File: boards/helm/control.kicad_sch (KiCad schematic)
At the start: 35 parts, among them J11 AS5600, J12 PICO UTIL, J13 THRUST DRV, J22 SERVO MOTOR, U1 Pico 2, U7 BTN8982TA, U8 BTN8982TA

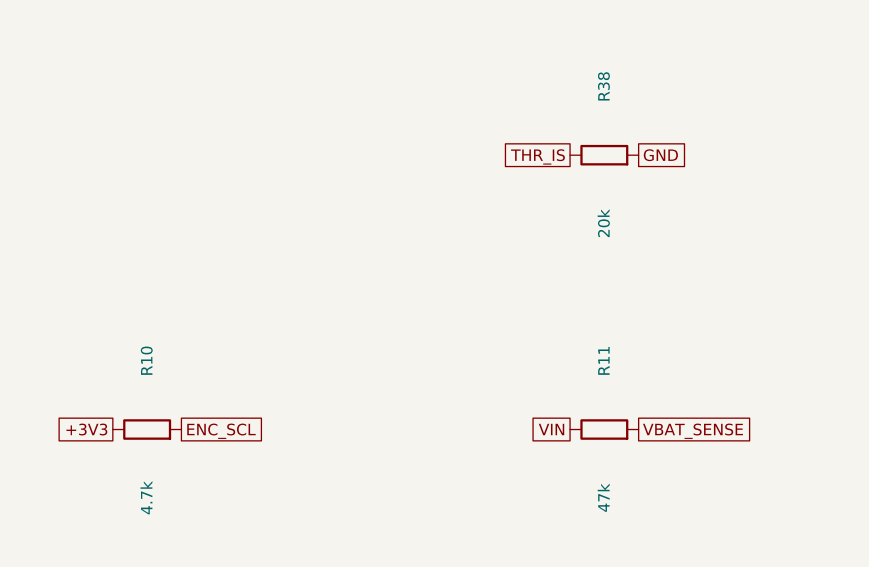
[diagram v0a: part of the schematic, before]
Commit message: feat(helm): steering-zero hall sensor input — J9 grows to 1x3 (5V/GND/SIG), 10k pullup + RC into Pico GP0
Open-collector hall switch (A3144 class) sees a magnet at servo center;
GP0 reads it (also broken out on J12.2; UART0 fallback = GP16/GP1).
Pour-redundant freerouted GND returns near J9/J10 removed. DRC 0/0.

Co-Authored-By: Claude Fable 5 <noreply@anthropic.com>
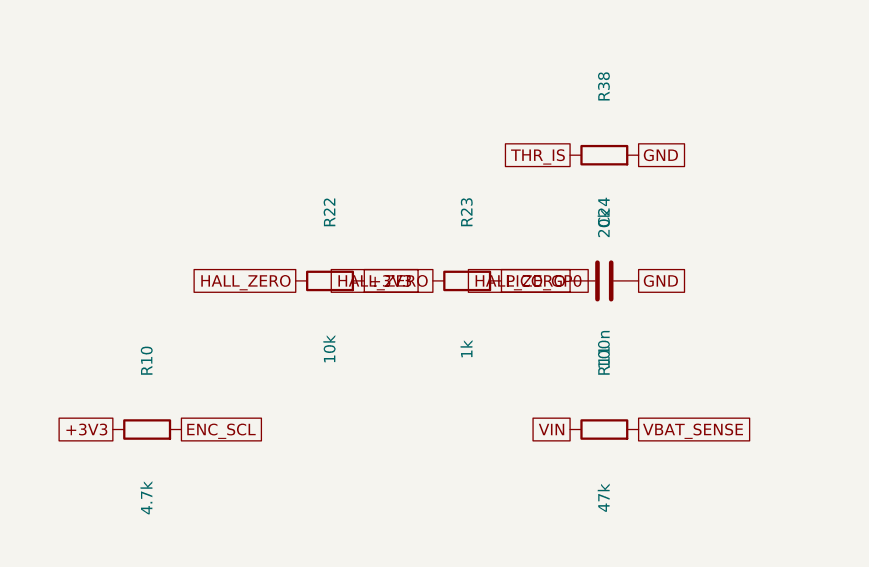
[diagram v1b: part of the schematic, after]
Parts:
- added C24: 100n, Capacitor_SMD:C_0805_2012Metric, symbol Device:C
- added R22: 10k, Resistor_SMD:R_0805_2012Metric, symbol Device:R
- added R23: 1k, Resistor_SMD:R_0805_2012Metric, symbol Device:R
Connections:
- net +3V3: now also R22.2
- net GND: now also C24.2
- net PICO_GP0: now also R23.2
- new net HALL_ZERO: C24.1, R22.1, R23.1
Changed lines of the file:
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@@
     (instances (project "vanchor-helm" (path "/a0000000-0000-4000-8000-000000000001/c0000000-0000-4000-8000-000000000004" (reference "LED5") (unit 1))))
+  )
+  (symbol (lib_id "Device:R") (at 165.1 195.58 90) (unit 1)
+    (exclude_from_sim no) (in_bom yes) (on_board yes) (dnp no)
+    (property "Reference" "R22" (at 165.1 187.96 0)
+      (effects (font (size 1.27 1.27))))
+    (property "Value" "10k" (at 165.1 203.2 0)
+      (effects (font (size 1.27 1.27))))
+    (property "Footprint" "Resistor_SMD:R_0805_2012Metric" (at 165.1 195.58 0)
+      (effects (font (size 1.27 1.27)) (hide yes)))
+    (property "Datasheet" "" (at 165.1 195.58 0)
+      (effects (font (size 1.27 1.27)) (hide yes)))
+    (pin "1")
+    (pin "2")
+    (instances (project "vanchor-helm" (path "/a0000000-0000-4000-8000-000000000001/c0000000-0000-4000-8000-000000000004" (reference "R22") (unit 1))))
+  )
+  (symbol (lib_id "Device:R") (at 180.34 195.58 90) (unit 1)
+    (exclude_from_sim no) (in_bom yes) (on_board yes) (dnp no)
+    (property "Reference" "R23" (at 180.34 187.96 0)
+      (effects (font (size 1.27 1.27))))
+    (property "Value" "1k" (at 180.34 203.2 0)
+      (effects (font (size 1.27 1.27))))
+    (property "Footprint" "Resistor_SMD:R_0805_2012Metric" (at 180.34 195.58 0)
+      (effects (font (size 1.27 1.27)) (hide yes)))
+    (property "Datasheet" "" (at 180.34 195.58 0)
+      (effects (font (size 1.27 1.27)) (hide yes)))
+    (pin "1")
+    (pin "2")
+    (instances (project "vanchor-helm" (path "/a0000000-0000-4000-8000-000000000001/c0000000-0000-4000-8000-000000000004" (reference "R23") (unit 1))))
+  )
+  (symbol (lib_id "Device:C") (at 195.58 195.58 90) (unit 1)
+    (exclude_from_sim no) (in_bom yes) (on_board yes) (dnp no)
+    (property "Reference" "C24" (at 195.58 187.96 0)
+      (effects (font (size 1.27 1.27))))
+    (property "Value" "100n" (at 195.58 203.2 0)
+      (effects (font (size 1.27 1.27))))
+    (property "Footprint" "Capacitor_SMD:C_0805_2012Metric" (at 195.58 195.58 0)
+      (effects (font (size 1.27 1.27)) (hide yes)))
+    (property "Datasheet" "" (at 195.58 195.58 0)
+      (effects (font (size 1.27 1.27)) (hide yes)))
+    (pin "1")
+    (pin "2")
+    (instances (project "vanchor-helm" (path "/a0000000-0000-4000-8000-000000000001/c0000000-0000-4000-8000-000000000004" (reference "C24") (unit 1))))
   )
   (symbol (lib_id "Connector_Generic:Conn_01x08") (at 195.58 100.33 0) (unit 1)
@@
       (effects (font (size 1.27 1.27)) (hide yes)))
   )
+  (global_label "HALL_ZERO" (shape passive) (at 161.29 195.58 180.0) (fields_autoplaced yes)
+    (effects (font (size 1.27 1.27)) (justify right))
+    (property "Intersheetrefs" "${INTERSHEET_REFS}" (at 161.29 195.58 0)
+      (effects (font (size 1.27 1.27)) (hide yes)))
+  )
+  (global_label "+3V3" (shape passive) (at 168.91 195.58 0.0) (fields_autoplaced yes)
+    (effects (font (size 1.27 1.27)) (justify left))
+    (property "Intersheetrefs" "${INTERSHEET_REFS}" (at 168.91 195.58 0)
+      (effects (font (size 1.27 1.27)) (hide yes)))
+  )
+  (global_label "HALL_ZERO" (shape passive) (at 176.53 195.58 180.0) (fields_autoplaced yes)
+    (effects (font (size 1.27 1.27)) (justify right))
+    (property "Intersheetrefs" "${INTERSHEET_REFS}" (at 176.53 195.58 0)
+      (effects (font (size 1.27 1.27)) (hide yes)))
+  )
+  (global_label "PICO_GP0" (shape passive) (at 184.15 195.58 0.0) (fields_autoplaced yes)
+    (effects (font (size 1.27 1.27)) (justify left))
+    (property "Intersheetrefs" "${INTERSHEET_REFS}" (at 184.15 195.58 0)
+      (effects (font (size 1.27 1.27)) (hide yes)))
+  )
+  (global_label "HALL_ZERO" (shape passive) (at 191.77 195.58 180.0) (fields_autoplaced yes)
+    (effects (font (size 1.27 1.27)) (justify right))
+    (property "Intersheetrefs" "${INTERSHEET_REFS}" (at 191.77 195.58 0)
+      (effects (font (size 1.27 1.27)) (hide yes)))
+  )
+  (global_label "GND" (shape passive) (at 199.39 195.58 0.0) (fields_autoplaced yes)
+    (effects (font (size 1.27 1.27)) (justify left))
+    (property "Intersheetrefs" "${INTERSHEET_REFS}" (at 199.39 195.58 0)
+      (effects (font (size 1.27 1.27)) (hide yes)))
+  )
